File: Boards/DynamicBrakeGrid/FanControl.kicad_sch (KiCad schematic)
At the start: 4 parts, among them M1 Fan_4pin, M2 Fan_4pin, M3 Fan_4pin, M8 Fan_4pin

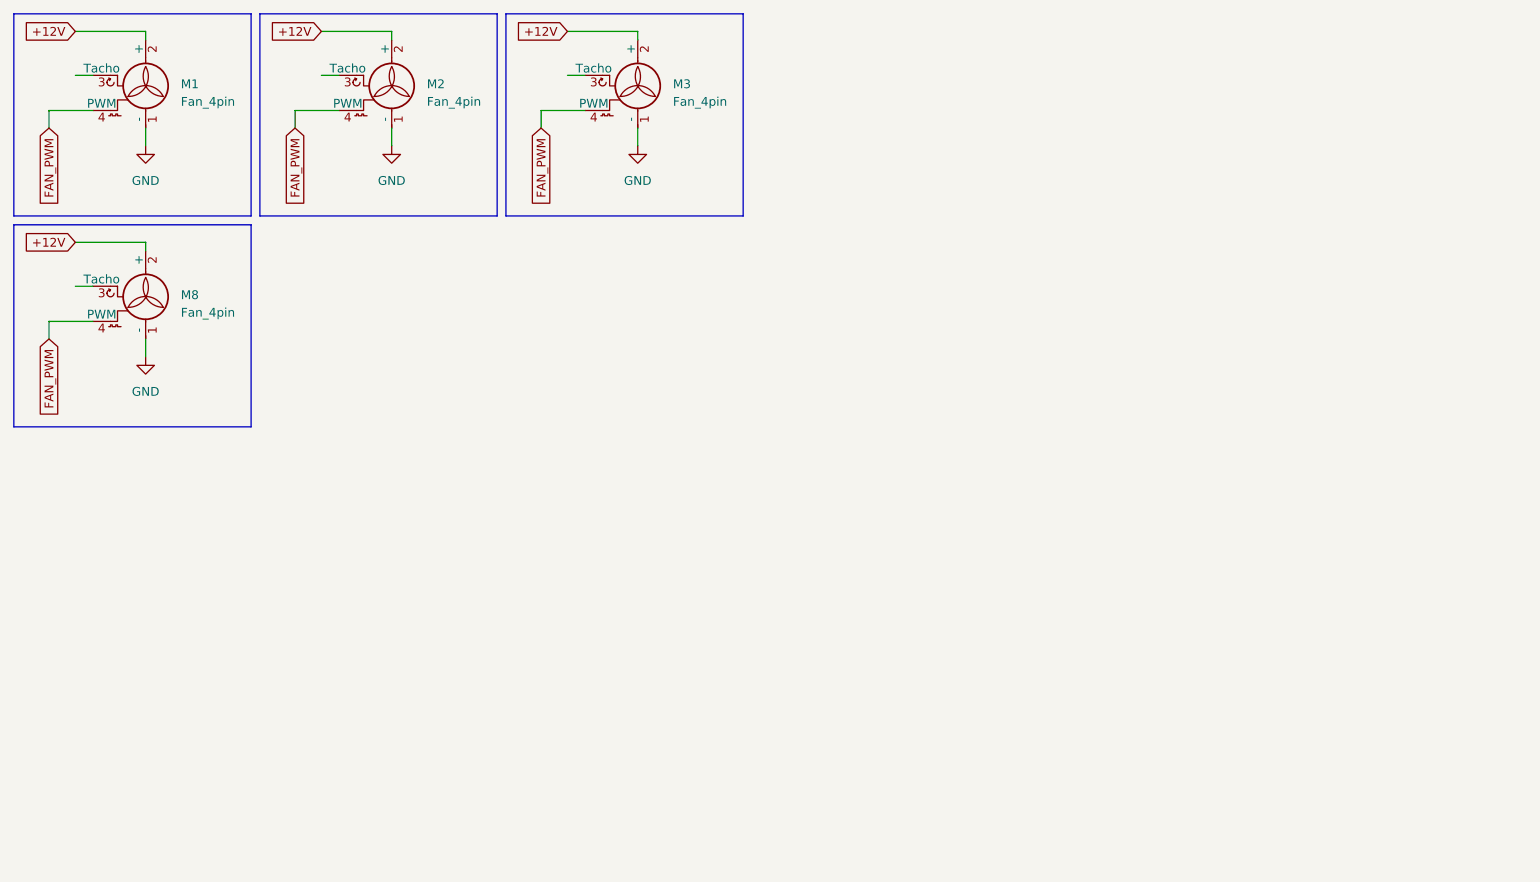
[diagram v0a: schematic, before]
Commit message: Update Dynamic Brake Board
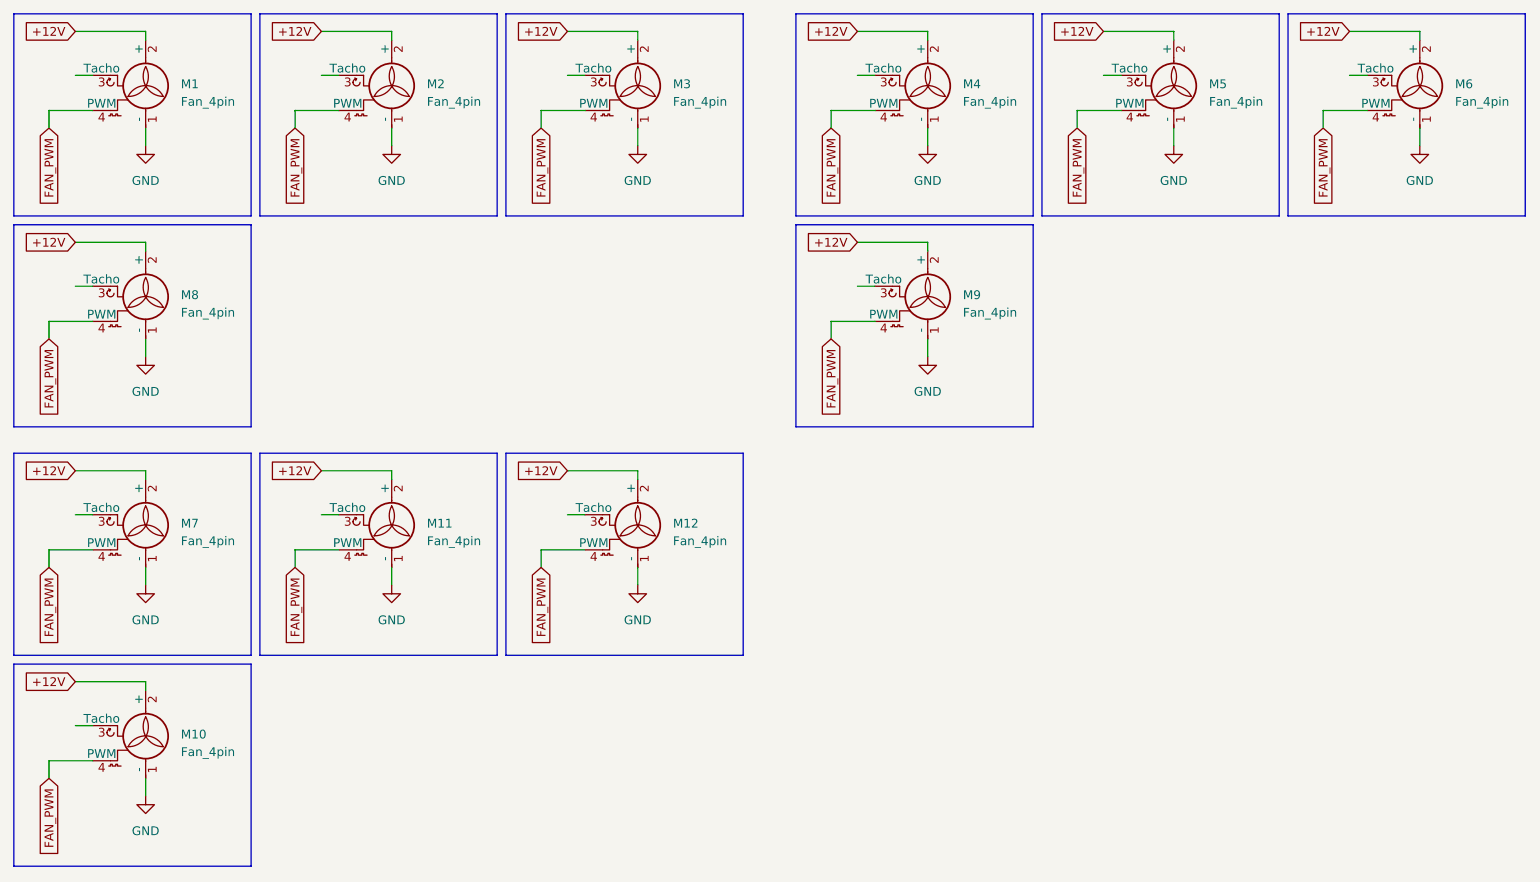
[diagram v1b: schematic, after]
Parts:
- added M10, M11, M12, M4, M5, M6, M7, M9: Fan_4pin, Connector:FanPinHeader_1x04_P2.54mm_Vertical, symbol Motor:Fan_4pin
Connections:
- net +12V: now also M10.2 (+), M11.2 (+), M12.2 (+), M4.2 (+), M5.2 (+), M6.2 (+), M7.2 (+), M9.2 (+)
- net FAN_PWM: now also M10.4 (PWM), M11.4 (PWM), M12.4 (PWM), M4.4 (PWM), M5.4 (PWM), M6.4 (PWM), M7.4 (PWM), M9.4 (PWM)
- net GND: now also M10.1 (-), M11.1 (-), M12.1 (-), M4.1 (-), M5.1 (-), M6.1 (-), M7.1 (-), M9.1 (-)
